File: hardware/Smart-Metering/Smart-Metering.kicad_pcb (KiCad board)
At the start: 4 copper layers, 130 x 130 mm, 230 parts, among them J101 AUX L N, J201 VA VB VC VN, J301 SENSOR_IA, J302 SENSOR_IB, J303 SENSOR_IC, J304 SENSOR_IN, J501 SWD, J701 HMI_LINK, J801 RS485, J802 USB-C, J901 BATTERY_1S, Q901 AO3401A, Q902 2N7002, SW901 POWER, U401 ADE9430ACPZ, U501 STM32F413RHT6, U502 24LC64, U601 ISO7762DW, U602 ISO7761DW, U604 MCP3204, U605 TPS7A2033PDBVR, U606 ADuM6000, U801 ADM2587E, U802 USBLC6-2SC6, U901 BQ25895RTW, U902 TPS63001, U903 TPS61022, Y401 24.576MHz, Y501 8MHz, Y502 32.768kHz

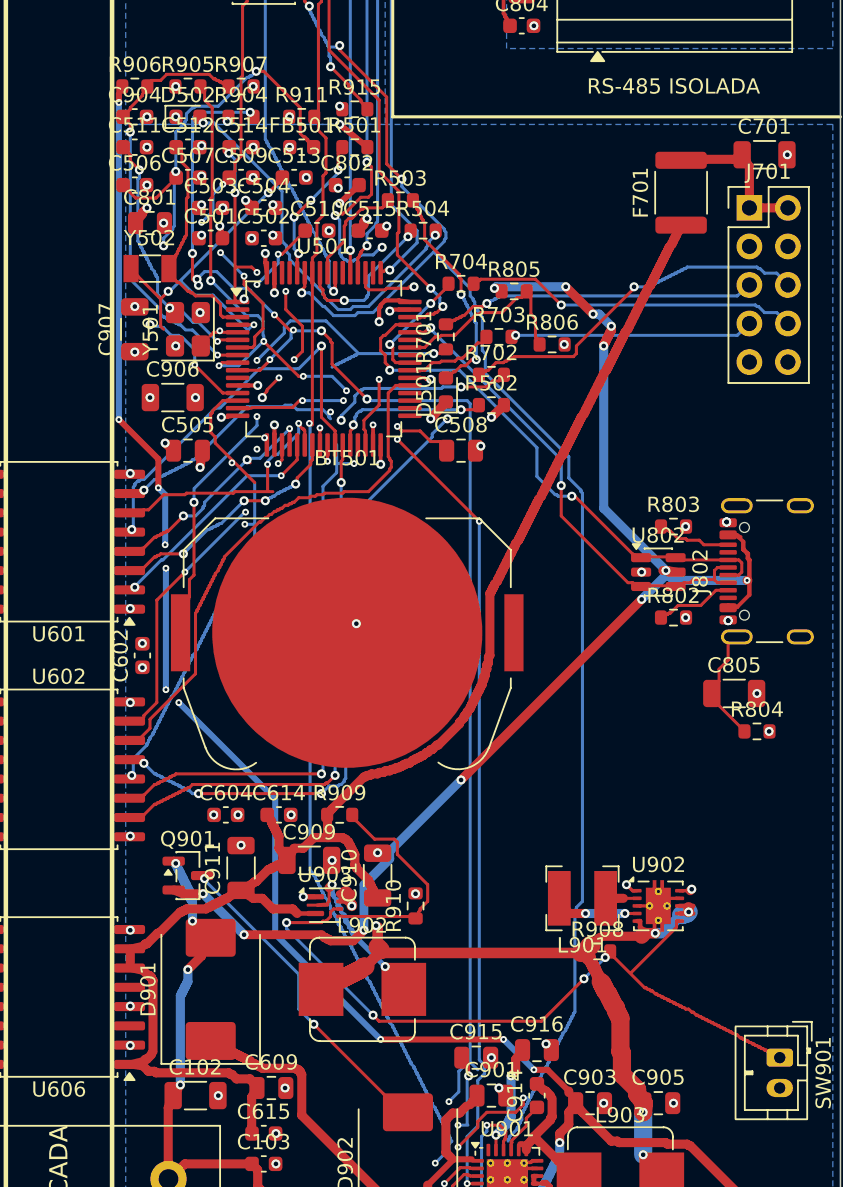
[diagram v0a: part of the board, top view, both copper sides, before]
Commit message: Aproxima o cristal do MCU e o indutor do boost de 5 V (layout rev. 0.6)
- Y501 girado 180° e C510/C511 a ~1,7 mm dos pads: HSE_IN 1,5 mm e
  HSE_OUT 5,4 mm, só na F.Cu e sem vias.
- C906/C907 (saída de +3V3) movidos para junto do U902.
- L902 junto do U903: SW_5V com 5,7 mm na F.Cu, sem vias (0,3 mm na saída
  do pino e 0,6 mm até o indutor); +5V do pino 3 por via de 0,6 mm.
- Trilhas sob os componentes movidos refeitas; 0 ligações abertas,
  0 violações e 8,02 mm na barreira.

Co-Authored-By: Claude Opus 5.5 <noreply@anthropic.com>
Claude-Session: https://claude.ai/code/session_012B8cVkhtjf3eg98UdpNCpf
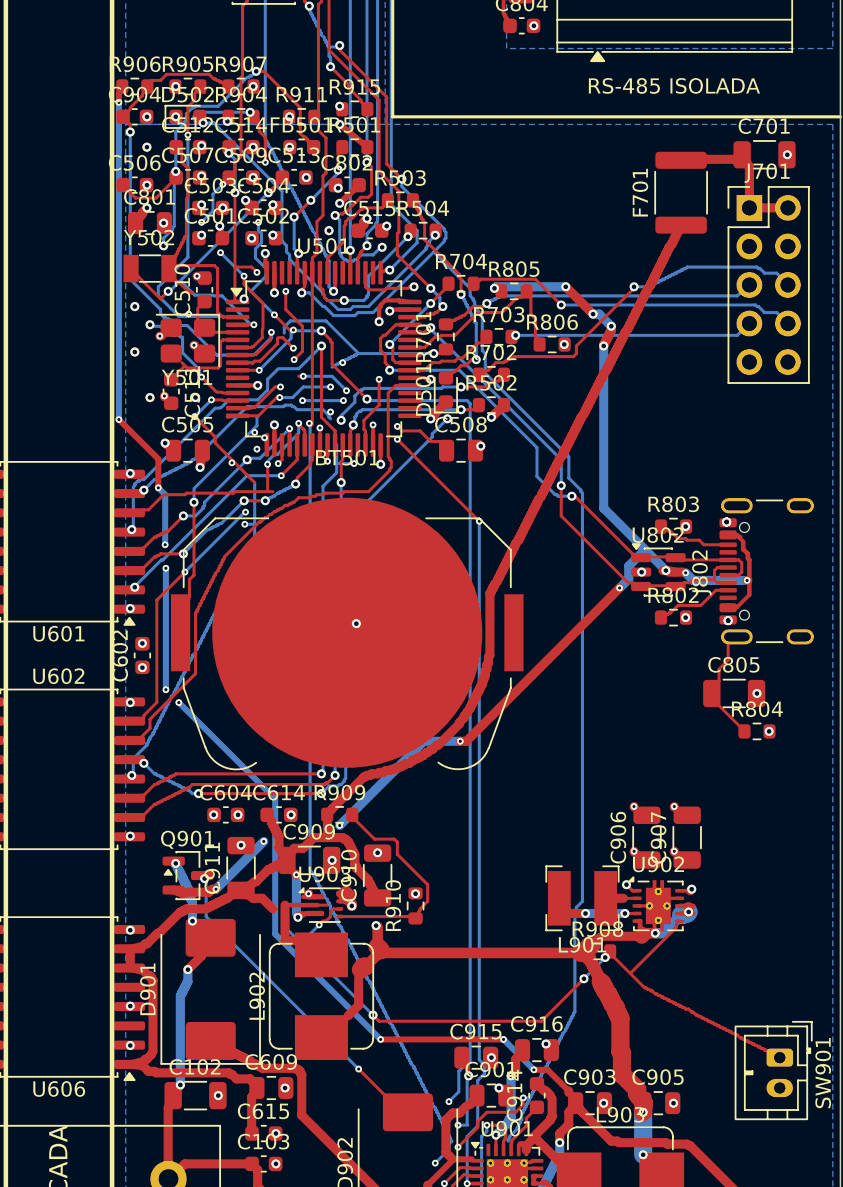
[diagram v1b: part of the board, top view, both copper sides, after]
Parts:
- moved C907 49.5 mm to (159.9, 111.5)
- moved C906 42.6 mm to (157.2, 111.5), turned to 90 degrees
- moved C511 16.3 mm to (125.9, 82.1), turned to 270 degrees
- moved C510 8.36 mm to (128.1, 75.4), turned to 90 degrees
- moved L902 2.74 mm to (135.8, 122.0), turned to 90 degrees
- moved Y501 0.75 mm to (127.0, 78.8), turned to 180 degrees
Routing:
- net /Metrology MCU/HSE_OUT: track 17.0 -> 5.41 mm, vias 3 -> 0
- net /Metrology MCU/HSE_IN: track 9.90 -> 1.50 mm, vias 3 -> 0
- net CHG_N: track 86.4 -> 93.9 mm
- net VBUS: track 86.3 -> 79.8 mm, vias 12 -> 13
- net /Metrology MCU/VBAT_RTC: track 40.9 -> 46.8 mm, vias 10 -> 8
- net VBAT_SENSE: track 28.1 -> 34.0 mm
- net CHG_INT_N: track 99.4 -> 94.5 mm, vias 11 -> 10
- net /Power Supplies/SW_5V: track 8.93 -> 5.70 mm, vias 2 -> 0
- net /Metrology MCU/LSE_IN: track 14.4 -> 17.5 mm
- net /Metrology MCU/LSE_OUT: track 22.8 -> 20.2 mm
- net +5V: track 104.3 -> 106.4 mm, vias 0 -> 2
- net MCU_CF1: track 35.9 -> 37.2 mm, vias 3 -> 5
- net MCU_CF2: track 48.0 -> 48.8 mm, vias 4 -> 5
- net /Power Supplies/PWR_EN: track 48.6 -> 48.1 mm
- net GND_SYS: track 31.6 -> 31.9 mm, vias 81 -> 85
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
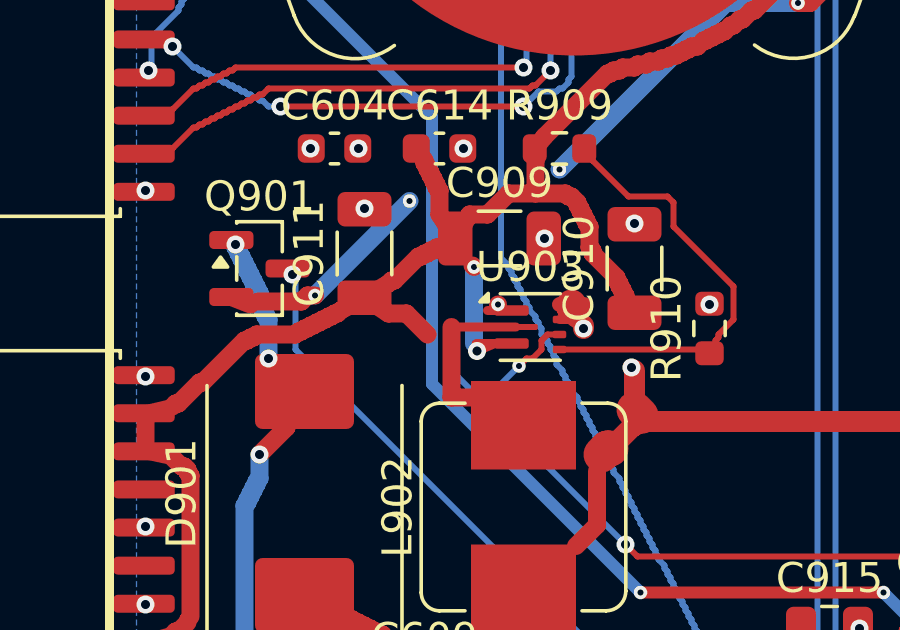
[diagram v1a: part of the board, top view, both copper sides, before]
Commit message: Alarga o SW_5V para 0,6 mm fora do courtyard do U903 e documenta a origem das posições
Resposta à revisão do PR #5: o trecho de 0,3 mm termina dentro do courtyard
(degrau de 0,4 mm na borda e 0,6 mm daí em diante); o +5V do pino 3 passa a
descer por duas vias de 0,45 mm. O LAYOUT deixa claro que o .kicad_pcb é a
fonte de verdade (o gerador não está no repositório).

Co-Authored-By: Claude Opus 5.5 <noreply@anthropic.com>
Claude-Session: https://claude.ai/code/session_012B8cVkhtjf3eg98UdpNCpf
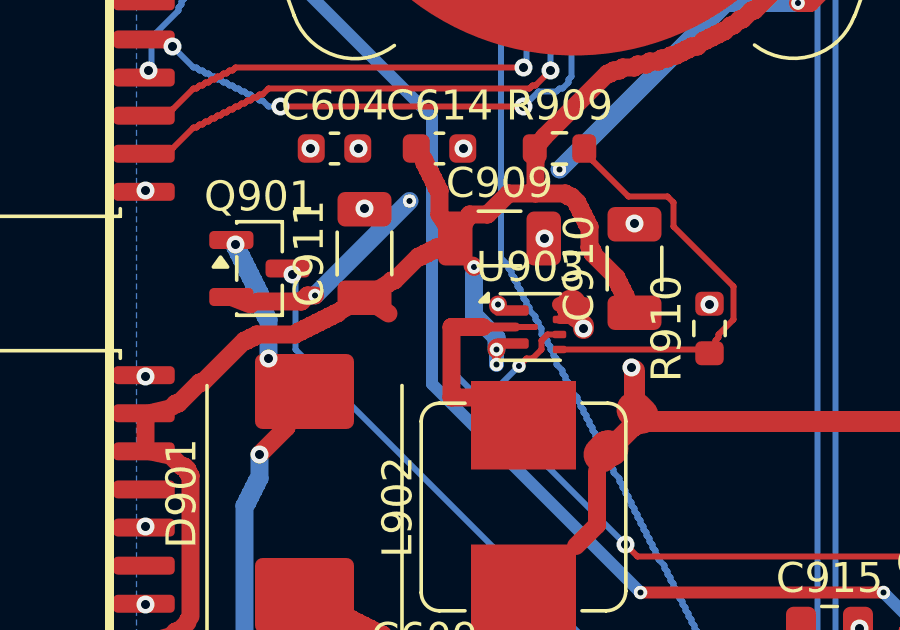
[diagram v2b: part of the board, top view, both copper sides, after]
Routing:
- net +5V: track 106.4 -> 104.3 mm, vias 2 -> 3
- net GND_SYS: track 31.9 -> 31.1 mm
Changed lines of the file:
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@@
 	)
 	(segment
-		(start 135.400 115.400)
-		(end 134.600 115.400)
-		(width 0.3)
-		(layer "F.Cu")
-		(net 67)
-	)
-	(segment
 		(start 127.725 72.000)
 		(end 127.900 71.800)
@@
 	)
 	(segment
-		(start 135.400 116.500)
-		(end 134.225 116.500)
-		(width 0.3)
-		(layer "F.Cu")
-		(net 3)
-	)
-	(segment
 		(start 131.200 128.600)
 		(end 131.200 130.600)
@@
 	(segment
 		(start 131.300 115.500)
-		(end 131.900 115.500)
-		(width 0.6)
-		(layer "F.Cu")
-		(net 3)
-	)
-	(segment
-		(start 131.900 115.500)
-		(end 132.600 116.200)
-		(width 0.6)
-		(layer "F.Cu")
-		(net 3)
-	)
-	(segment
-		(start 131.300 115.500)
 		(end 130.500 114.975)
 		(width 0.6)
@@
 	)
 	(segment
-		(start 135.550 115.950)
-		(end 133.400 115.950)
-		(width 0.3)
-		(layer "F.Cu")
-		(net 56)
-	)
-	(segment
-		(start 133.400 115.950)
-		(end 133.400 118.300)
-		(width 0.6)
-		(layer "F.Cu")
-		(net 56)
-	)
-	(segment
-		(start 133.400 118.300)
-		(end 134.600 118.300)
-		(width 0.6)
-		(layer "F.Cu")
-		(net 56)
-	)
-	(segment
-		(start 135.400 116.500)
-		(end 134.850 116.500)
-		(width 0.3)
-		(layer "F.Cu")
-		(net 3)
-	)
-	(segment
-		(start 134.850 116.500)
-		(end 134.250 116.750)
-		(width 0.3)
-		(layer "F.Cu")
-		(net 3)
-	)
-	(segment
-		(start 134.150 116.500)
-		(end 134.150 113.950)
-		(width 0.6)
-		(layer "B.Cu")
-		(net 3)
-	)
-	(segment
 		(start 134.150 113.950)
 		(end 134.100 113.900)
@@
 		(net 64)
 	)
+	(segment
+		(start 135.550 115.950)
+		(end 134.600 115.950)
+		(width 0.3)
+		(layer "F.Cu")
+		(net 56)
+	)
+	(segment
+		(start 134.600 115.950)
+		(end 134.450 115.950)
+		(width 0.4)
+		(layer "F.Cu")
+		(net 56)
+	)
+	(segment
+		(start 134.450 115.950)
+		(end 133.400 115.950)
+		(width 0.6)
+		(layer "F.Cu")
+		(net 56)
+	)
+	(segment
+		(start 133.400 115.950)
+		(end 133.400 118.300)
+		(width 0.6)
+		(layer "F.Cu")
+		(net 56)
+	)
+	(segment
+		(start 133.400 118.300)
+		(end 134.600 118.300)
+		(width 0.6)
+		(layer "F.Cu")
+		(net 56)
+	)
+	(segment
+		(start 135.400 116.500)
+		(end 134.850 116.500)
+		(width 0.3)
+		(layer "F.Cu")
+		(net 3)
+	)
+	(segment
+		(start 134.900 116.650)
+		(end 134.900 116.700)
+		(width 0.6)
+		(layer "F.Cu")
+		(net 3)
+	)
+	(segment
+		(start 134.900 116.700)
+		(end 134.900 116.300)
+		(width 0.6)
+		(layer "B.Cu")
+		(net 3)
+	)
+	(segment
+		(start 134.900 116.300)
+		(end 134.150 115.550)
+		(width 0.6)
+		(layer "B.Cu")
+		(net 3)
+	)
+	(segment
+		(start 134.150 115.550)
+		(end 134.150 114.150)
+		(width 0.6)
+		(layer "B.Cu")
+		(net 3)
+	)
+	(segment
+		(start 134.900 116.700)
+		(end 134.900 117.200)
+		(width 0.3)
+		(layer "F.Cu")
+		(net 3)
+	)
+	(segment
+		(start 134.900 116.700)
+		(end 134.900 117.200)
+		(width 0.5)
+		(layer "B.Cu")
+		(net 3)
+	)
 	(via
 		(at 153.200 116.500)
@@
 	)
 	(via
-		(at 134.250 116.750)
-		(size 0.6)
-		(drill 0.3)
-		(layers "F.Cu" "B.Cu")
-		(net 3)
-	)
-	(via
 		(at 134.150 113.950)
 		(size 0.45)
@@
 		(net 64)
 	)
+	(via
+		(at 134.900 116.700)
+		(size 0.45)
+		(drill 0.2)
+		(layers "F.Cu" "B.Cu")
+		(net 3)
+	)
+	(via
+		(at 134.900 117.200)
+		(size 0.45)
+		(drill 0.2)
+		(layers "F.Cu" "B.Cu")
+		(net 3)
+	)
 )

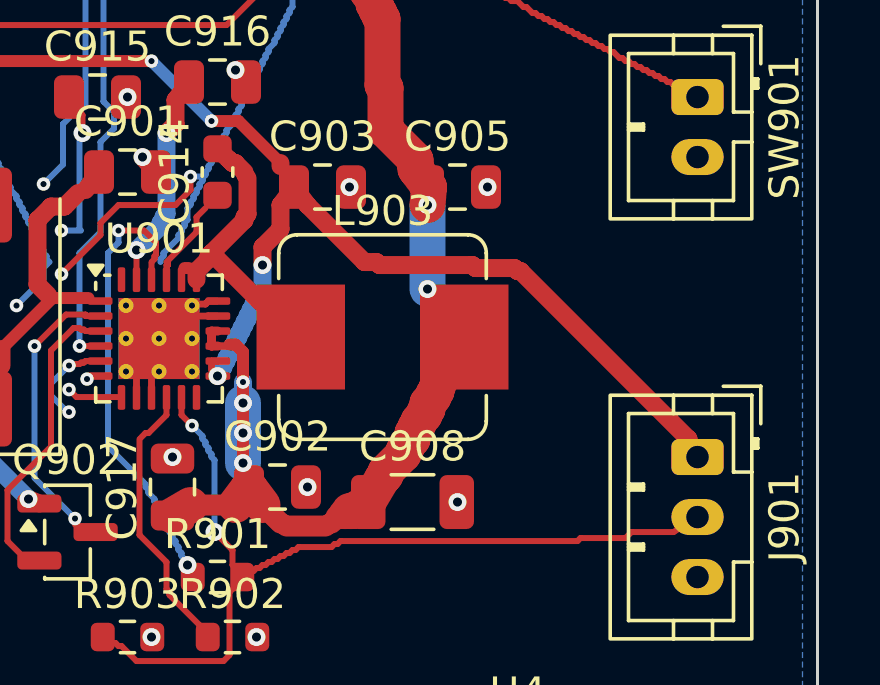
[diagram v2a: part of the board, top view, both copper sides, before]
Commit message: Alarga a saída VSYS do U901 (L903 deslocado 1 mm)
- L903 movido 1 mm para a direita, abrindo espaço entre os pinos SYS do
  BQ25895 e o pad CHG_SW.
- Saída VSYS: 0,75 mm sobre os pinos 15/16 e 1,2 mm na F.Cu até o C902,
  em paralelo com o caminho de 1,2 mm na B.Cu.
- CHG_SW e VBAT religados; 0 ligações abertas, 0 violações e 8,02 mm na
  barreira.

Co-Authored-By: Claude Opus 5.5 <noreply@anthropic.com>
Claude-Session: https://claude.ai/code/session_012B8cVkhtjf3eg98UdpNCpf
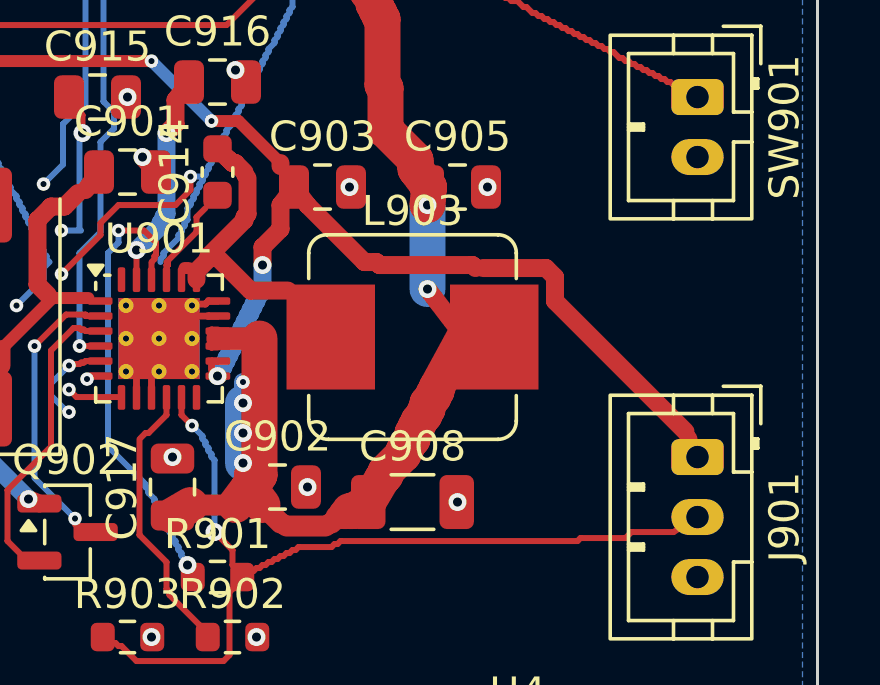
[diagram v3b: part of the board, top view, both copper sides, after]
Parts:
- moved L903 1.00 mm to (156.5, 134.0)
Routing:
- net /Power Supplies/VSYS: track 75.6 -> 77.7 mm
- net /Power Supplies/CHG_SW: track 9.79 -> 8.50 mm
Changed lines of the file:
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@@
 	(footprint "Inductor_SMD:L_Bourns_SRP7028A_7.3x6.6mm"
 		(layer "F.Cu")
-		(at 155.500 134.000 0)
+		(at 156.500 134.000 0)
 		(descr "Shielded Power Inductors (https://www.bourns.com/docs/product-datasheets/srp7028a.pdf)")
 		(tags "Shielded Inductors Bourns SMD SRP7028A")
@@
 	)
 	(segment
-		(start 158.600 131.700)
-		(end 159.900 131.700)
-		(width 0.6)
-		(layer "F.Cu")
-		(net 57)
-	)
-	(segment
-		(start 159.900 131.700)
-		(end 160.000 131.800)
-		(width 0.6)
-		(layer "F.Cu")
-		(net 57)
-	)
-	(segment
-		(start 160.000 131.800)
-		(end 160.100 131.800)
-		(width 0.6)
-		(layer "F.Cu")
-		(net 57)
-	)
-	(segment
-		(start 160.100 131.800)
-		(end 165.700 137.400)
-		(width 0.6)
-		(layer "F.Cu")
-		(net 57)
-	)
-	(segment
 		(start 165.700 137.400)
 		(end 165.700 137.500)
@@
 	)
 	(segment
-		(start 149.800 131.200)
-		(end 151.400 132.800)
-		(width 0.6)
-		(layer "F.Cu")
-		(net 50)
-	)
-	(segment
-		(start 151.400 132.800)
-		(end 152.775 134.000)
-		(width 0.6)
-		(layer "F.Cu")
-		(net 50)
-	)
-	(segment
 		(start 137.100 116.700)
 		(end 141.600 116.700)
@@
 	)
 	(segment
-		(start 150.400 134.250)
-		(end 150.600 134.250)
-		(width 0.4)
-		(layer "F.Cu")
-		(net 60)
-	)
-	(segment
-		(start 150.600 134.250)
-		(end 150.850 134.500)
-		(width 0.4)
-		(layer "F.Cu")
-		(net 60)
-	)
-	(segment
-		(start 150.850 134.500)
-		(end 150.850 138.300)
-		(width 0.4)
-		(layer "F.Cu")
-		(net 60)
-	)
-	(segment
 		(start 163.900 94.550)
 		(end 163.850 94.550)
@@
 		(net 3)
 	)
+	(segment
+		(start 165.600 137.150)
+		(end 161.250 132.800)
+		(width 0.6)
+		(layer "F.Cu")
+		(net 57)
+	)
+	(segment
+		(start 161.250 132.800)
+		(end 161.250 132.000)
+		(width 0.6)
+		(layer "F.Cu")
+		(net 57)
+	)
+	(segment
+		(start 161.250 132.000)
+		(end 160.950 131.700)
+		(width 0.6)
+		(layer "F.Cu")
+		(net 57)
+	)
+	(segment
+		(start 160.950 131.700)
+		(end 158.850 131.700)
+		(width 0.6)
+		(layer "F.Cu")
+		(net 57)
+	)
+	(segment
+		(start 150.000 134.050)
+		(end 151.400 134.050)
+		(width 0.75)
+		(layer "F.Cu")
+		(net 60)
+	)
+	(segment
+		(start 151.400 134.050)
+		(end 151.400 138.600)
+		(width 1.2)
+		(layer "F.Cu")
+		(net 60)
+	)
+	(segment
+		(start 151.400 138.600)
+		(end 151.050 139.000)
+		(width 1.2)
+		(layer "F.Cu")
+		(net 60)
+	)
+	(segment
+		(start 152.350 132.450)
+		(end 151.100 132.450)
+		(width 0.6)
+		(layer "F.Cu")
+		(net 50)
+	)
+	(segment
+		(start 151.100 132.450)
+		(end 150.000 131.350)
+		(width 0.6)
+		(layer "F.Cu")
+		(net 50)
+	)
 	(via
